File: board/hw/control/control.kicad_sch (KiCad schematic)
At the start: 40 parts

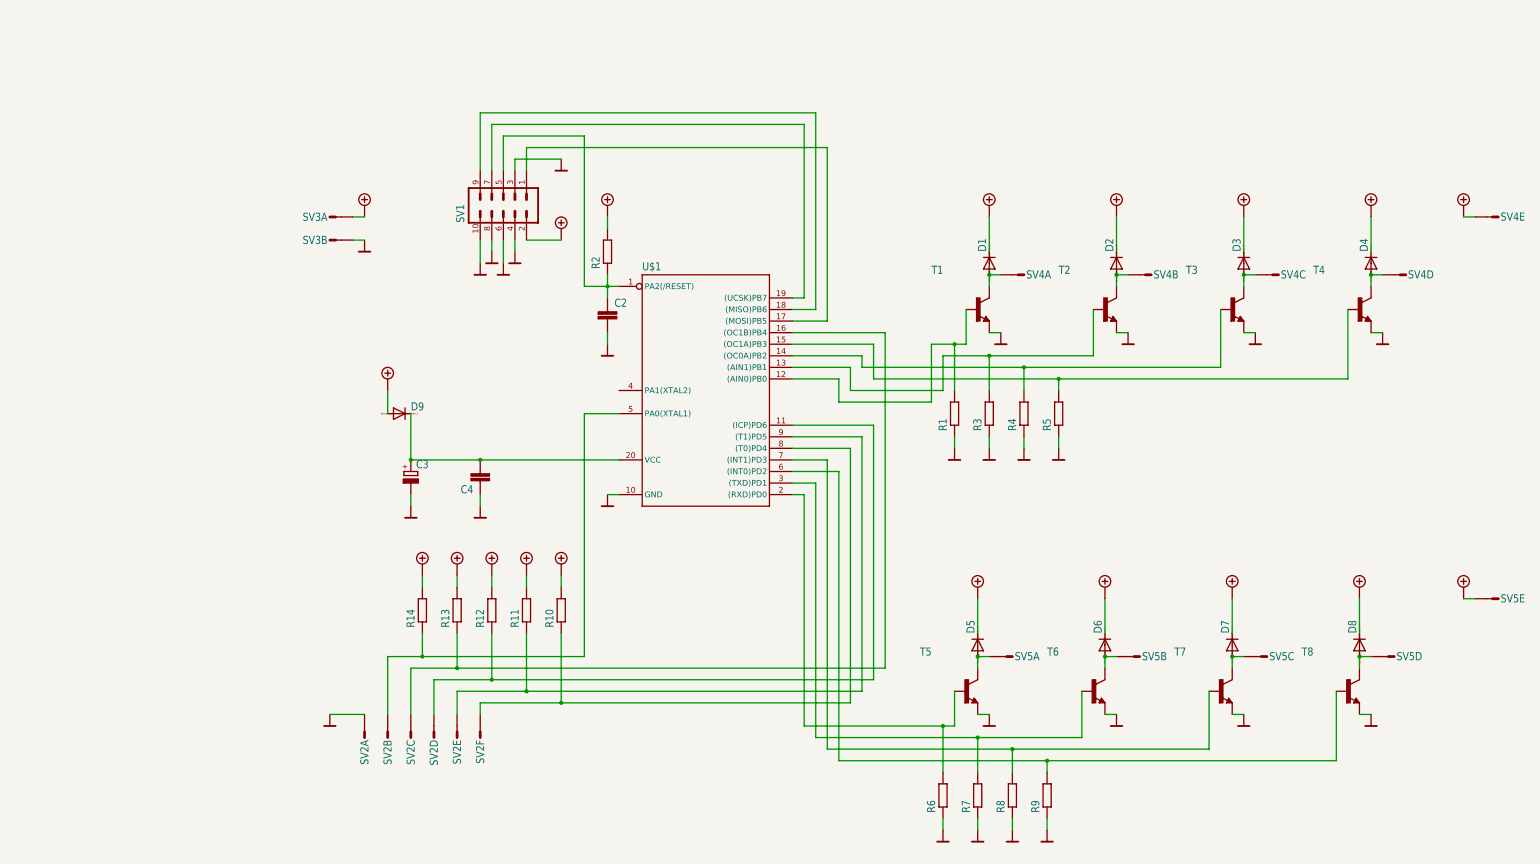
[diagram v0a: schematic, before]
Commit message: ctrl board coverted to newer KiCad
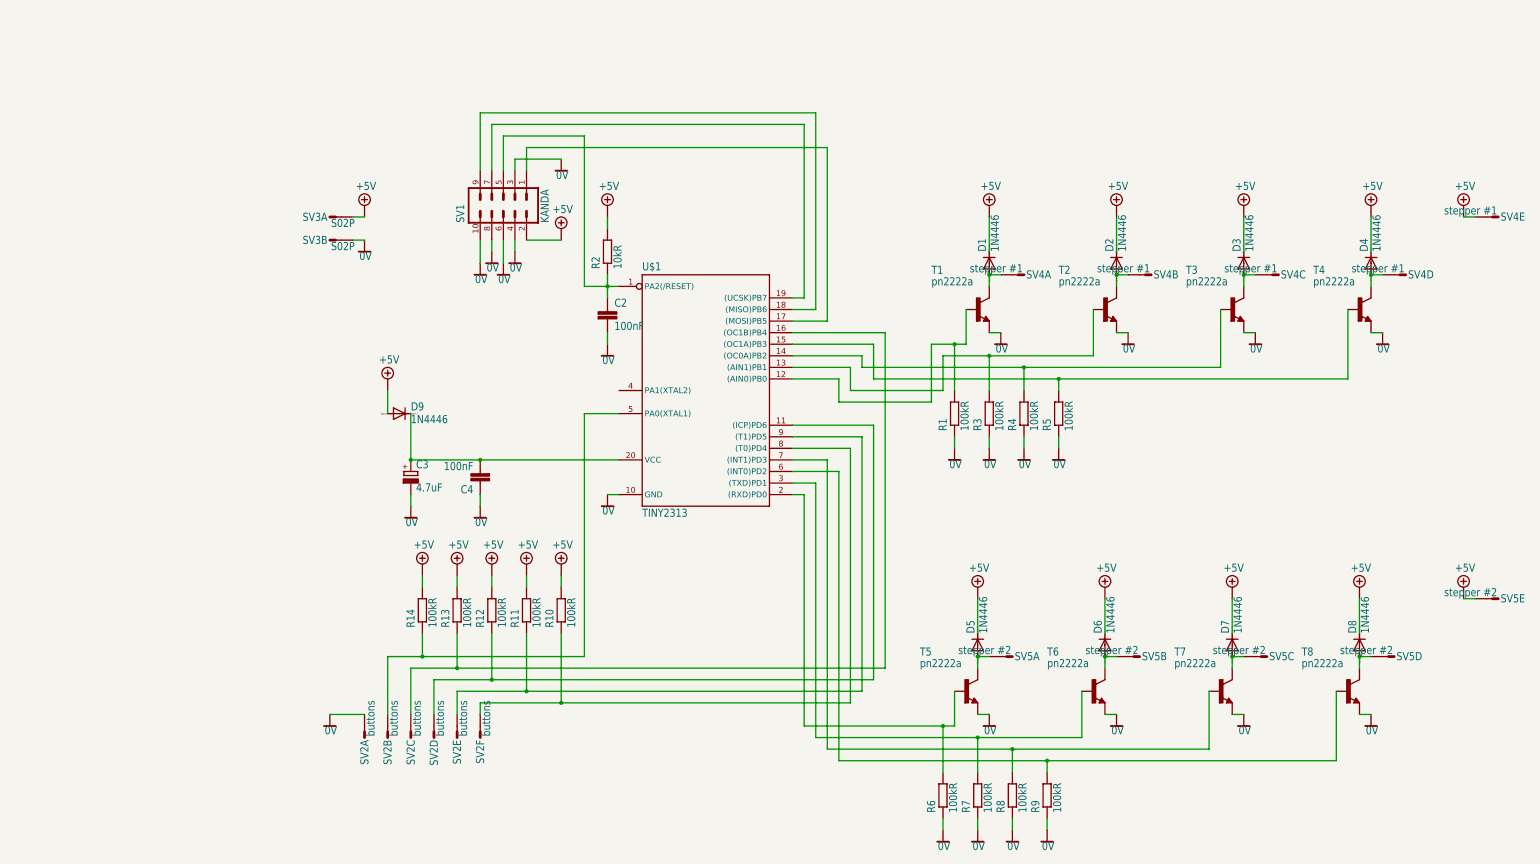
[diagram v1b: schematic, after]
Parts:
- C2, C4: value (none) -> 100nF; footprint (none) -> control:C3216
- C3: value (none) -> 4.7uF; footprint (none) -> control:153CLV-0405
- D1, D2, D3, D4, D5, D6, D7, D8, D9: value (none) -> 1N4446; footprint (none) -> control:DO35-10
- R1, R10, R11, R12, R13, R14, R3, R4, R5, R6, R7, R8, R9: value (none) -> 100kR; footprint (none) -> control:MINI_MELF-0204W
- R2: value (none) -> 10kR; footprint (none) -> control:MINI_MELF-0204W
- SV1: value (none) -> KANDA; footprint (none) -> control:ML10
- SV2: value (none) -> buttons; footprint (none) -> control:S06P
- SV3: value (none) -> S02P; footprint (none) -> control:S02P
- SV4: value (none) -> stepper #1; footprint (none) -> control:S05P
- SV5: value (none) -> stepper #2; footprint (none) -> control:S05P
- T1, T2, T3, T4, T5, T6, T7, T8: value (none) -> pn2222a; footprint (none) -> control:TO92-CBE
- U$1: value (none) -> TINY2313; footprint (none) -> control:DIL20

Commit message: moved most elements from Eagle to KiCad libraries
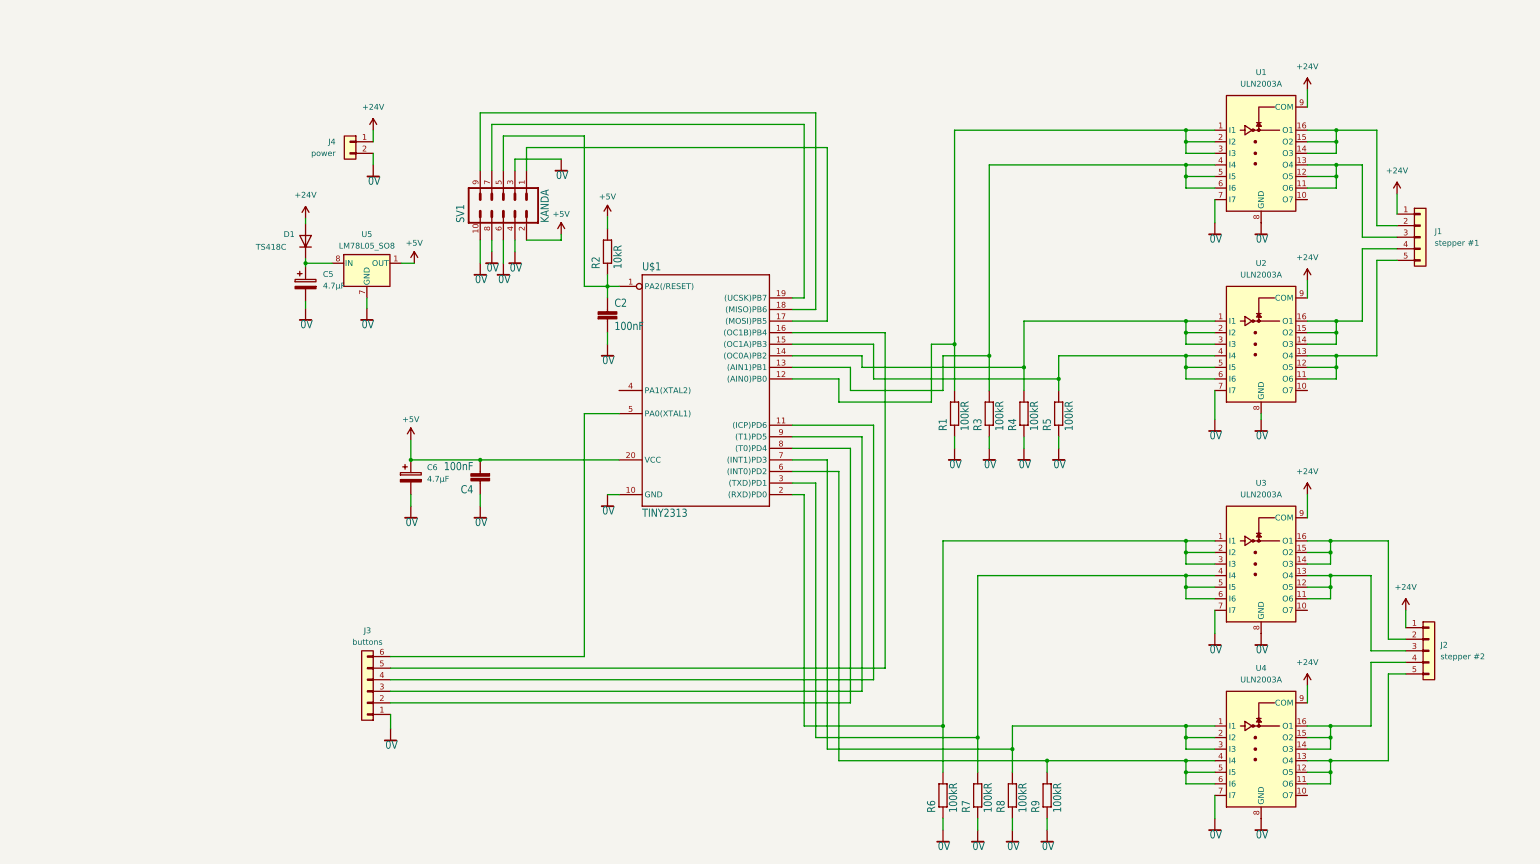
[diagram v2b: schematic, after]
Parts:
- removed C3: 4.7uF, control:153CLV-0405, symbol control-eagle-import:CPOL-EU153CLV-0405
- removed D1, D2, D3, D4, D5, D6, D7, D8, D9: 1N4446, control:DO35-10, symbol control-eagle-import:1N4446
- removed R10, R11, R12, R13, R14: 100kR, control:MINI_MELF-0204W, symbol control-eagle-import:R-EU_MELF0204W
- removed SV2: buttons, control:S06P, symbol control-eagle-import:S06P
- removed SV3: S02P, control:S02P, symbol control-eagle-import:S02P
- removed SV4: stepper #1, control:S05P, symbol control-eagle-import:S05P
- removed SV5: stepper #2, control:S05P, symbol control-eagle-import:S05P
- removed T1, T2, T3, T4, T5, T6, T7, T8: pn2222a, control:TO92-CBE, symbol control-eagle-import:-NPN-TO92-CBE
- added C5, C6: 4.7µF, Capacitor_SMD:CP_Elec_4x5.8, symbol Device:C_Polarized
- added D1: TS418C, Diode_SMD:D_0805_2012Metric, symbol Diode:CD4148W
- added J1: stepper #1, Connector_PinSocket_2.54mm:PinSocket_1x05_P2.54mm_Vertical, symbol Connector_Generic:Conn_01x05
- added J2: stepper #2, Connector_PinSocket_2.54mm:PinSocket_1x05_P2.54mm_Vertical, symbol Connector_Generic:Conn_01x05
- added J3: buttons, Connector_PinSocket_2.54mm:PinSocket_1x06_P2.54mm_Vertical, symbol Connector_Generic:Conn_01x06
- added J4: power, Connector_PinSocket_2.54mm:PinSocket_1x02_P2.54mm_Vertical, symbol Connector_Generic:Conn_01x02
- added U1: ULN2003A, Package_SO:SOIC-16_3.9x9.9mm_P1.27mm, symbol Transistor_Array:ULN2003A
- added U2, U3, U4: ULN2003A, Package_SO:SOIC-16_3.9x9.9mm_P1.27mm, symbol Transistor_Array:ULN2003
- added U5: LM78L05_SO8, Package_SO:SOIC-8_3.9x4.9mm_P1.27mm, symbol Regulator_Linear:LM78L05_SO8
- C2: footprint control:C3216 -> Capacitor_SMD:C_0805_2012Metric
- C4: footprint control:C3216 -> Capacitor_SMD:C_0805_2012Metric_Pad1.18x1.45mm_HandSolder
- R1, R2, R3, R4, R5, R6, R7, R8, R9: footprint control:MINI_MELF-0204W -> Resistor_SMD:R_0805_2012Metric_Pad1.20x1.40mm_HandSolder
- U$1: footprint control:DIL20 -> Package_SO:SOIC-20W_7.5x12.8mm_P1.27mm
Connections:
- net +5V: now also U5.1 (OUT)
- net 0V: now also C5.2, C6.2, J3.1 (Pin_1), J4.2 (Pin_2), U1.7 (I7), U1.8 (GND), U2.7 (I7), U2.8 (GND), U3.7 (I7), U3.8 (GND), U4.7 (I7), U4.8 (GND), U5.2 (GND), U5.3 (GND), U5.6 (GND), U5.7 (GND)
- net at R4.2, U$1.14 ((OC0A)PB2): now also U2.1 (I1), U2.2 (I2), U2.3 (I3)
- net at C4.2, U$1.20 (VCC): now also C6.1
- net at U$1.9 ((T1)PD5): now also J3.3 (Pin_3)
- net at U$1.11 ((ICP)PD6): now also J3.4 (Pin_4)
- net at R8.2, U$1.7 ((INT1)PD3): now also U4.1 (I1), U4.2 (I2), U4.3 (I3)
- net at R5.2, U$1.15 ((OC1A)PB3): now also U2.4 (I4), U2.5 (I5), U2.6 (I6)
- net at R6.2, U$1.2 ((RXD)PD0): now also U3.1 (I1), U3.2 (I2), U3.3 (I3)
- net at U$1.16 ((OC1B)PB4): now also J3.5 (Pin_5)
- net at R3.2, U$1.13 ((AIN1)PB1): now also U1.4 (I4), U1.5 (I5), U1.6 (I6)
- net at R9.2, U$1.6 ((INT0)PD2): now also U4.4 (I4), U4.5 (I5), U4.6 (I6)
- net at U$1.8 ((T0)PD4): now also J3.2 (Pin_2)
- net at U$1.5 (PA0(XTAL1)): now also J3.6 (Pin_6)
- net at R7.2, U$1.3 ((TXD)PD1): now also U3.4 (I4), U3.5 (I5), U3.6 (I6)
- net at R1.2, U$1.12 ((AIN0)PB0): now also U1.1 (I1), U1.2 (I2), U1.3 (I3)
- new net: C5.1, D1.1 (K), U5.8 (IN)
- new net: J1.5 (Pin_5), U2.11 (O6), U2.12 (O5), U2.13 (O4)
- new net: J1.4 (Pin_4), U2.14 (O3), U2.15 (O2), U2.16 (O1)
- new net: J1.3 (Pin_3), U1.11 (O6), U1.12 (O5), U1.13 (O4)
- new net: J1.2 (Pin_2), U1.14 (O3), U1.15 (O2), U1.16 (O1)
- new net: J2.2 (Pin_2), U3.14 (O3), U3.15 (O2), U3.16 (O1)
- new net: J2.3 (Pin_3), U3.11 (O6), U3.12 (O5), U3.13 (O4)
- new net: J2.4 (Pin_4), U4.14 (O3), U4.15 (O2), U4.16 (O1)
- new net: J2.5 (Pin_5), U4.11 (O6), U4.12 (O5), U4.13 (O4)
- new net +24V: D1.2 (A), J1.1 (Pin_1), J2.1 (Pin_1), J4.1 (Pin_1), U1.9 (COM), U2.9 (COM), U3.9 (COM), U4.9 (COM)

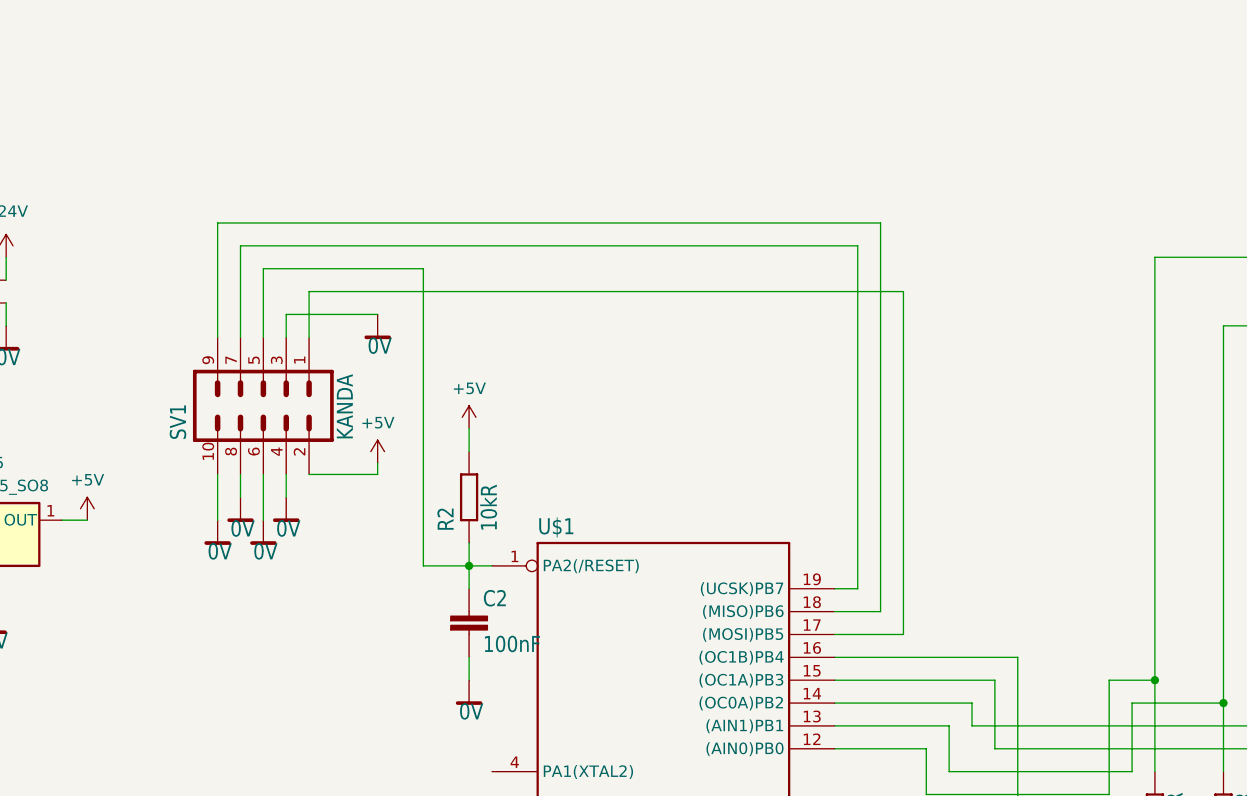
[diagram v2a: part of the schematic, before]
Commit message: removed unused elements and added proper AVR-ISP-10 conector
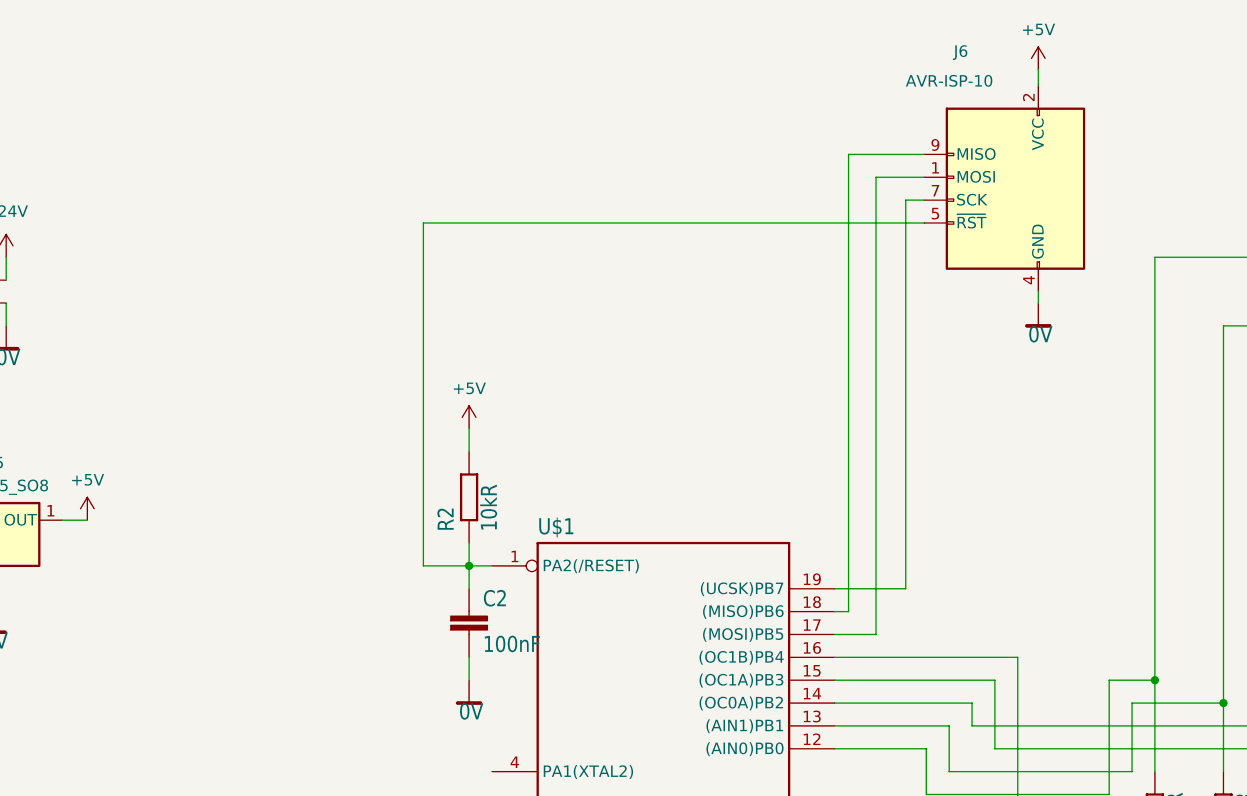
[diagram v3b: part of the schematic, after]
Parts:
- removed SV1: KANDA, control:ML10, symbol control-eagle-import:ML10
- added J6: AVR-ISP-10, Connector_IDC:IDC-Header_2x05_P2.54mm_Vertical, symbol Connector:AVR-ISP-10
- J1, J2: footprint Connector_PinSocket_2.54mm:PinSocket_1x05_P2.54mm_Vertical -> Connector_PinHeader_2.54mm:PinHeader_1x05_P2.54mm_Vertical
- J4: footprint Connector_PinSocket_2.54mm:PinSocket_1x02_P2.54mm_Vertical -> Connector_PinHeader_2.54mm:PinHeader_1x02_P2.54mm_Vertical
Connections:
- net +5V: now also J6.2 (VCC)
- net 0V: now also J6.10 (GND), J6.4 (GND), J6.6 (GND), J6.8 (GND)
- net at U$1.17 ((MOSI)PB5): now also J6.1 (MOSI)
- net at C2.1, R2.1, U$1.1 (PA2(/RESET)): now also J6.5 (~{RST})
- net at U$1.19 ((UCSK)PB7): now also J6.7 (SCK)
- net at U$1.18 ((MISO)PB6): now also J6.9 (MISO)
